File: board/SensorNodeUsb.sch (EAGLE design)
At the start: 18 parts, among them X2 USBPCB

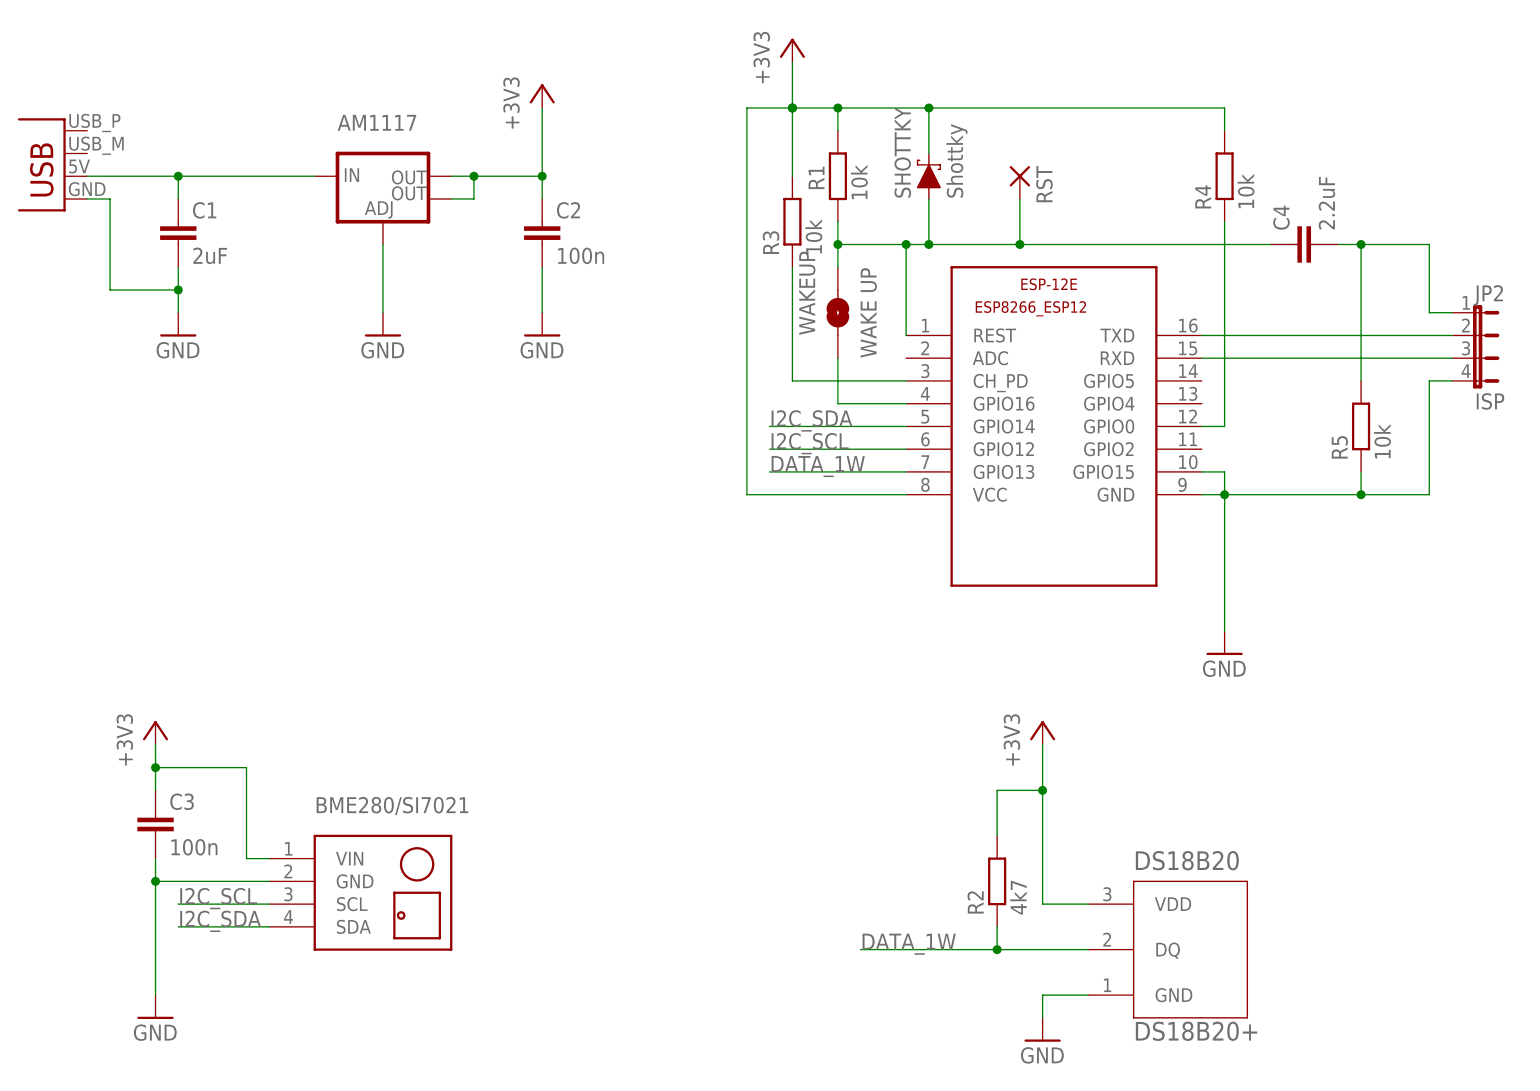
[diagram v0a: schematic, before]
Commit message: modify adjust a part name and a part value
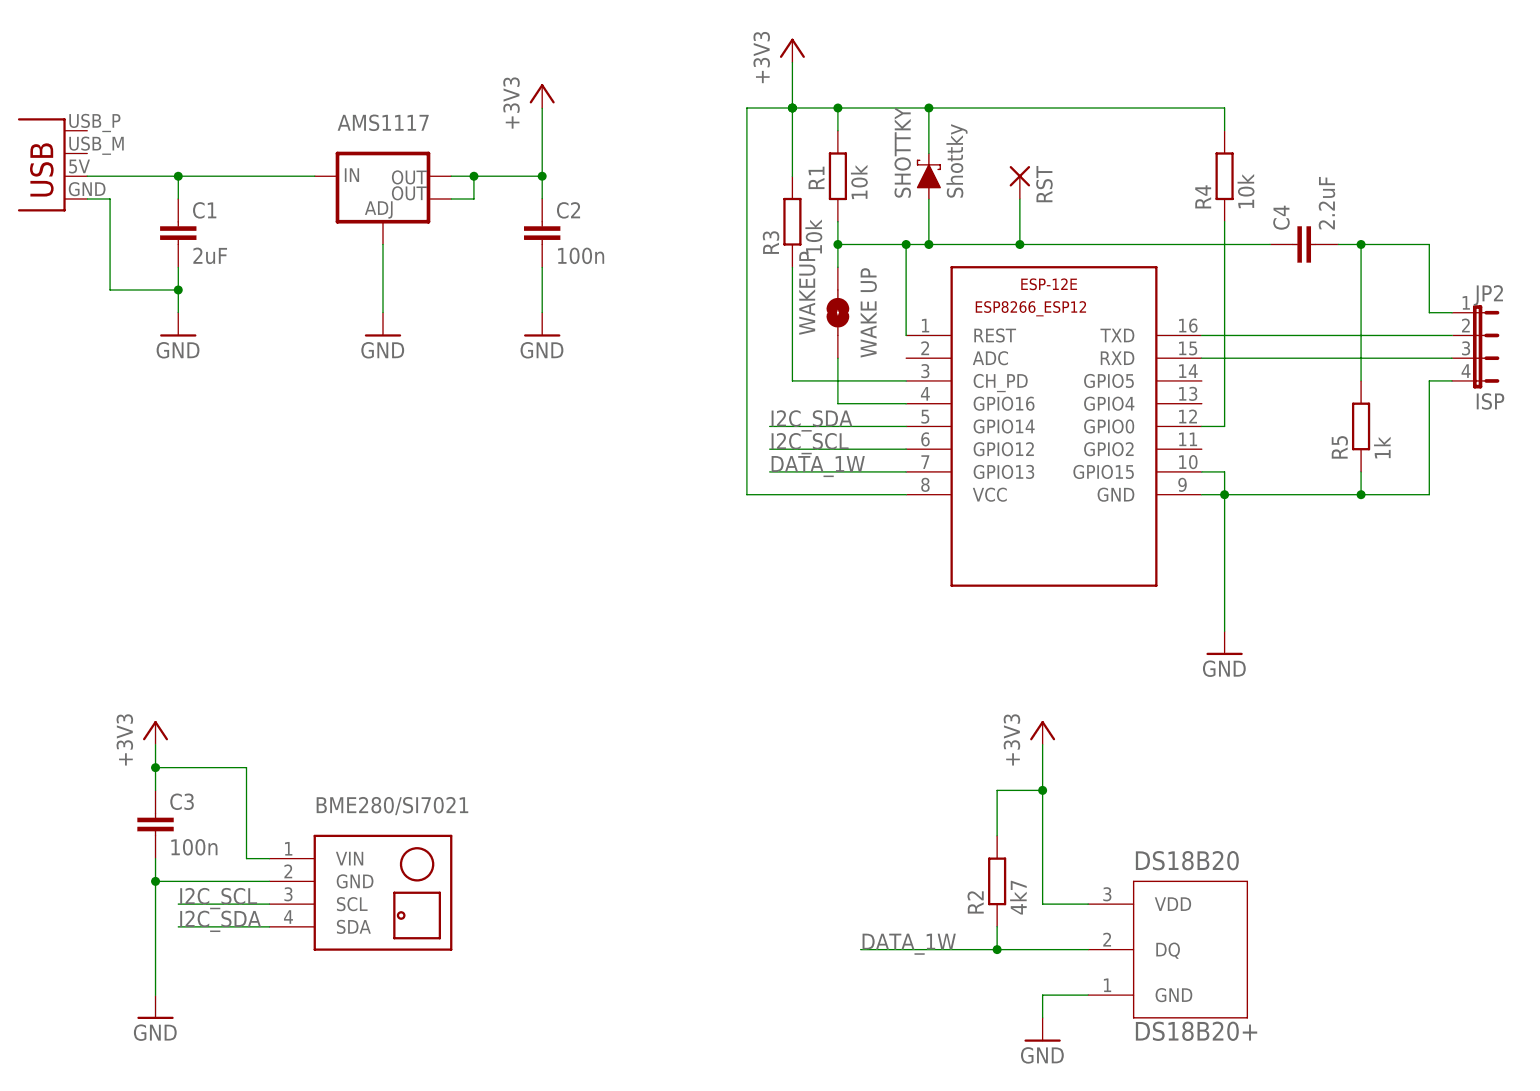
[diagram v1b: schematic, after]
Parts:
- R5: value 10k -> 1k
- renumbered AM1117 to AMS1117
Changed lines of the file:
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@@
 <grid distance="0.1" unitdist="inch" unit="inch" style="lines" multiple="1" display="no" altdistance="0.01" altunitdist="inch" altunit="inch"/>
 <layers>
-<layer number="1" name="Top" color="4" fill="1" visible="yes" active="no"/>
-<layer number="16" name="Bottom" color="1" fill="1" visible="yes" active="no"/>
-<layer number="17" name="Pads" color="2" fill="1" visible="yes" active="no"/>
-<layer number="18" name="Vias" color="2" fill="1" visible="yes" active="no"/>
-<layer number="19" name="Unrouted" color="6" fill="1" visible="yes" active="no"/>
-<layer number="20" name="Dimension" color="24" fill="1" visible="yes" active="no"/>
-<layer number="21" name="tPlace" color="7" fill="1" visible="yes" active="no"/>
-<layer number="22" name="bPlace" color="7" fill="1" visible="yes" active="no"/>
-<layer number="23" name="tOrigins" color="15" fill="1" visible="yes" active="no"/>
-<layer number="24" name="bOrigins" color="15" fill="1" visible="yes" active="no"/>
-<layer number="25" name="tNames" color="7" fill="1" visible="yes" active="no"/>
-<layer number="26" name="bNames" color="7" fill="1" visible="yes" active="no"/>
-<layer number="27" name="tValues" color="7" fill="1" visible="yes" active="no"/>
-<layer number="28" name="bValues" color="7" fill="1" visible="yes" active="no"/>
+<layer number="1" name="Top" color="4" fill="1" visible="no" active="no"/>
+<layer number="16" name="Bottom" color="1" fill="1" visible="no" active="no"/>
+<layer number="17" name="Pads" color="2" fill="1" visible="no" active="no"/>
+<layer number="18" name="Vias" color="2" fill="1" visible="no" active="no"/>
+<layer number="19" name="Unrouted" color="6" fill="1" visible="no" active="no"/>
+<layer number="20" name="Dimension" color="24" fill="1" visible="no" active="no"/>
+<layer number="21" name="tPlace" color="7" fill="1" visible="no" active="no"/>
+<layer number="22" name="bPlace" color="7" fill="1" visible="no" active="no"/>
+<layer number="23" name="tOrigins" color="15" fill="1" visible="no" active="no"/>
+<layer number="24" name="bOrigins" color="15" fill="1" visible="no" active="no"/>
+<layer number="25" name="tNames" color="7" fill="1" visible="no" active="no"/>
+<layer number="26" name="bNames" color="7" fill="1" visible="no" active="no"/>
+<layer number="27" name="tValues" color="7" fill="1" visible="no" active="no"/>
+<layer number="28" name="bValues" color="7" fill="1" visible="no" active="no"/>
 <layer number="29" name="tStop" color="7" fill="3" visible="no" active="no"/>
 <layer number="30" name="bStop" color="7" fill="6" visible="no" active="no"/>
@@
 <layer number="35" name="tGlue" color="7" fill="4" visible="no" active="no"/>
 <layer number="36" name="bGlue" color="7" fill="5" visible="no" active="no"/>
-<layer number="37" name="tTest" color="7" fill="1" visible="yes" active="no"/>
-<layer number="38" name="bTest" color="7" fill="1" visible="yes" active="no"/>
+<layer number="37" name="tTest" color="7" fill="1" visible="no" active="no"/>
+<layer number="38" name="bTest" color="7" fill="1" visible="no" active="no"/>
 <layer number="39" name="tKeepout" color="4" fill="11" visible="no" active="no"/>
 <layer number="40" name="bKeepout" color="1" fill="11" visible="no" active="no"/>
@@
 <layer number="44" name="Drills" color="7" fill="1" visible="no" active="no"/>
 <layer number="45" name="Holes" color="7" fill="1" visible="no" active="no"/>
-<layer number="46" name="Milling" color="3" fill="1" visible="yes" active="no"/>
-<layer number="47" name="Measures" color="7" fill="1" visible="yes" active="no"/>
-<layer number="48" name="Document" color="7" fill="1" visible="yes" active="no"/>
-<layer number="49" name="Reference" color="7" fill="1" visible="yes" active="no"/>
-<layer number="50" name="dxf" color="7" fill="1" visible="yes" active="no"/>
-<layer number="51" name="tDocu" color="7" fill="1" visible="yes" active="no"/>
-<layer number="52" name="bDocu" color="7" fill="1" visible="yes" active="no"/>
-<layer number="53" name="tGND_GNDA" color="7" fill="9" visible="yes" active="no"/>
-<layer number="54" name="bGND_GNDA" color="1" fill="9" visible="yes" active="no"/>
-<layer number="56" name="wert" color="7" fill="1" visible="yes" active="no"/>
-<layer number="57" name="tCAD" color="7" fill="1" visible="yes" active="no"/>
-<layer number="59" name="tCarbon" color="7" fill="1" visible="yes" active="no"/>
-<layer number="60" name="bCarbon" color="7" fill="1" visible="yes" active="no"/>
+<layer number="46" name="Milling" color="3" fill="1" visible="no" active="no"/>
+<layer number="47" name="Measures" color="7" fill="1" visible="no" active="no"/>
+<layer number="48" name="Document" color="7" fill="1" visible="no" active="no"/>
+<layer number="49" name="Reference" color="7" fill="1" visible="no" active="no"/>
+<layer number="50" name="dxf" color="7" fill="1" visible="no" active="no"/>
+<layer number="51" name="tDocu" color="7" fill="1" visible="no" active="no"/>
+<layer number="52" name="bDocu" color="7" fill="1" visible="no" active="no"/>
+<layer number="53" name="tGND_GNDA" color="7" fill="9" visible="no" active="no"/>
+<layer number="54" name="bGND_GNDA" color="1" fill="9" visible="no" active="no"/>
+<layer number="56" name="wert" color="7" fill="1" visible="no" active="no"/>
+<layer number="57" name="tCAD" color="7" fill="1" visible="no" active="no"/>
+<layer number="59" name="tCarbon" color="7" fill="1" visible="no" active="no"/>
+<layer number="60" name="bCarbon" color="7" fill="1" visible="no" active="no"/>
 <layer number="88" name="SimResults" color="9" fill="1" visible="yes" active="yes"/>
 <layer number="89" name="SimProbes" color="9" fill="1" visible="yes" active="yes"/>
@@
 <part name="DS18B20" library="thomo" deviceset="DS18B20+" device="" value="DS18B20+"/>
 <part name="SHOTTKY" library="SparkFun-DiscreteSemi" library_urn="urn:adsk.eagle:library:514" deviceset="DIODE-SCHOTTKY" device="-B340A" package3d_urn="urn:adsk.eagle:package:38443/1" value="Shottky"/>
-<part name="AM1117" library="SparkFun-IC-Power" library_urn="urn:adsk.eagle:library:526" deviceset="V_REG_LM1117" device="SOT223" package3d_urn="urn:adsk.eagle:package:39069/1"/>
+<part name="AMS1117" library="SparkFun-IC-Power" library_urn="urn:adsk.eagle:library:526" deviceset="V_REG_LM1117" device="SOT223" package3d_urn="urn:adsk.eagle:package:39069/1"/>
 <part name="WAKEUP" library="SparkFun-Jumpers" library_urn="urn:adsk.eagle:library:528" deviceset="JUMPER-SMT_2_NO" device="_SILK" package3d_urn="urn:adsk.eagle:package:39279/1" value="WAKE UP"/>
 <part name="JP2" library="jumper" library_urn="urn:adsk.eagle:library:252" deviceset="JP4E" device="" package3d_urn="urn:adsk.eagle:package:15463/1" value="ISP"/>
 <part name="C4" library="rcl" library_urn="urn:adsk.eagle:library:334" deviceset="C-EU" device="C1206" package3d_urn="urn:adsk.eagle:package:23618/2" value="2.2uF"/>
-<part name="R5" library="rcl" library_urn="urn:adsk.eagle:library:334" deviceset="R-EU_" device="M1206" package3d_urn="urn:adsk.eagle:package:23566/2" value="10k"/>
+<part name="R5" library="rcl" library_urn="urn:adsk.eagle:library:334" deviceset="R-EU_" device="M1206" package3d_urn="urn:adsk.eagle:package:23566/2" value="1k"/>
 <part name="RST" library="wirepad" library_urn="urn:adsk.eagle:library:412" deviceset="2,15/1,0" device="" package3d_urn="urn:adsk.eagle:package:30831/1"/>
 <part name="C3" library="rcl" library_urn="urn:adsk.eagle:library:334" deviceset="C-EU" device="C1206K" package3d_urn="urn:adsk.eagle:package:23682/2" value="100n"/>
@@
 <attribute name="VALUE" x="151.892" y="139.7" size="1.778" layer="96" font="vector" rot="R90" align="top-left"/>
 </instance>
-<instance part="AM1117" gate="G$1" x="88.9" y="142.24" smashed="yes">
+<instance part="AMS1117" gate="G$1" x="88.9" y="142.24" smashed="yes">
 <attribute name="NAME" x="83.82" y="147.32" size="1.778" layer="95" font="vector"/>
 <attribute name="VALUE" x="83.82" y="147.32" size="1.778" layer="96" font="vector"/>
@@
 </segment>
 <segment>
-<pinref part="AM1117" gate="G$1" pin="ADJ"/>
+<pinref part="AMS1117" gate="G$1" pin="ADJ"/>
 <pinref part="GND9" gate="1" pin="GND"/>
 <wire x1="88.9" y1="127" x2="88.9" y2="134.62" width="0.1524" layer="91"/>
@@
 </segment>
 <segment>
-<pinref part="AM1117" gate="G$1" pin="OUT@1"/>
+<pinref part="AMS1117" gate="G$1" pin="OUT@1"/>
 <wire x1="96.52" y1="139.7" x2="99.06" y2="139.7" width="0.1524" layer="91"/>
 <wire x1="99.06" y1="139.7" x2="99.06" y2="142.24" width="0.1524" layer="91"/>
-<pinref part="AM1117" gate="G$1" pin="OUT"/>
+<pinref part="AMS1117" gate="G$1" pin="OUT"/>
 <wire x1="96.52" y1="142.24" x2="99.06" y2="142.24" width="0.1524" layer="91"/>
 <pinref part="C2" gate="G$1" pin="1"/>
@@
 <wire x1="66.04" y1="139.7" x2="66.04" y2="142.24" width="0.1524" layer="91"/>
 <junction x="66.04" y="142.24"/>
-<pinref part="AM1117" gate="G$1" pin="IN"/>
+<pinref part="AMS1117" gate="G$1" pin="IN"/>
 <wire x1="66.04" y1="142.24" x2="81.28" y2="142.24" width="0.1524" layer="91"/>
 <pinref part="X2" gate="G$1" pin="VBUS"/>

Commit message: 5-pin programming interface
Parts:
- removed C4: 2.2uF, rcl:C-EUC1206
- removed JP2: ISP, jumper:JP4E
- removed RST: (no value), wirepad:2,15/1,0
- removed SHOTTKY: Shottky, SparkFun-DiscreteSemi:DIODE-SCHOTTKY-B340A
- added J1: JP5E, thomo:JP5E
- R5: value 1k -> 10k
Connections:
- removed net N$1: C4.1, ESP-12E.REST, R1.2, RST.P, SHOTTKY.A, WAKEUP.2
- removed net N$4: ESP-12E.GPIO0, R4.1
- removed net N$5: C4.2, JP2.1, R5.2
- removed net N$6: ESP-12E.TXD, JP2.2
- removed net N$7: ESP-12E.RXD, JP2.3
- new net DTR: ESP-12E.GPIO0, J1.1, R4.1
- new net N$9: ESP-12E.GPIO15, R5.2
- new net RST: ESP-12E.REST, J1.2, R1.2, WAKEUP.2
- new net RX: ESP-12E.RXD, J1.4
- new net TX: ESP-12E.TXD, J1.3
- net +3V3: no longer SHOTTKY.C
- net GND: now also J1.5; no longer ESP-12E.GPIO15, JP2.4
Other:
- moved on the sheet: R5
